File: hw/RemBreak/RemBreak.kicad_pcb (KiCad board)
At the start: 11 copper layers, 40 x 80 mm, 78 parts, among them IC1 LTC2943IDD#TRPBF, J1 Conn_01x03, J10 Screw_Terminal_01x02, J11 Conn_01x03, J2 Conn_02x06_Odd_Even, J3 Screw_Terminal_01x04, J5 Screw_Terminal_01x04, J8 Conn_01x07, J9 Conn_01x07, Q1 BC337, Q11 BC337, Q12 BC847, Q2 BC847, Q3 BC847, Q4 BC337, Q5 BC847, Q6 BC337, Q7 BC847, Q8 SiS415DNT, Q9 BC337, U1 L7805, U2 L7805, U3 XC6220B331MR, U4 MAX40200AUK, U5 INA219BxDCN, U7 MAX40200AUK, U8 BD48ExxG, U9 BD48ExxG

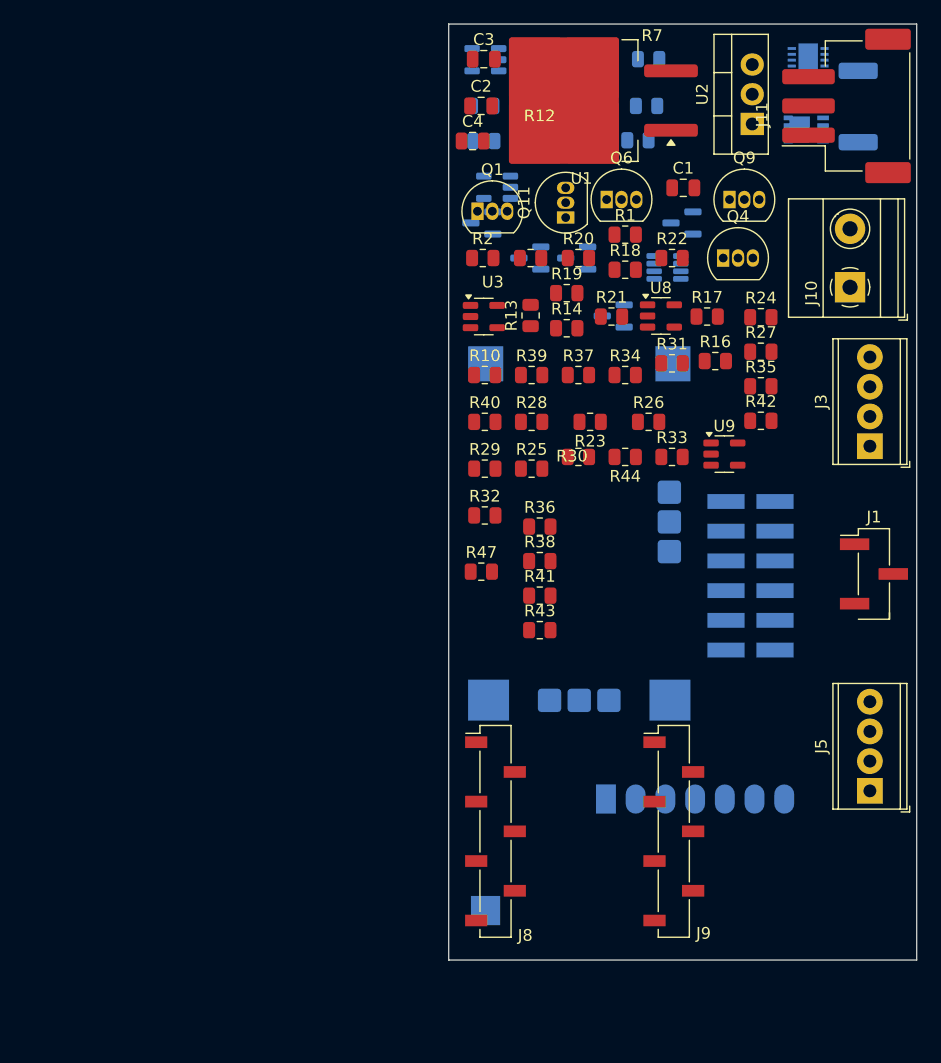
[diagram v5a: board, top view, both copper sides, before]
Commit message: created 3mm band around the pcb and components grouped to be easily placed in the final layout
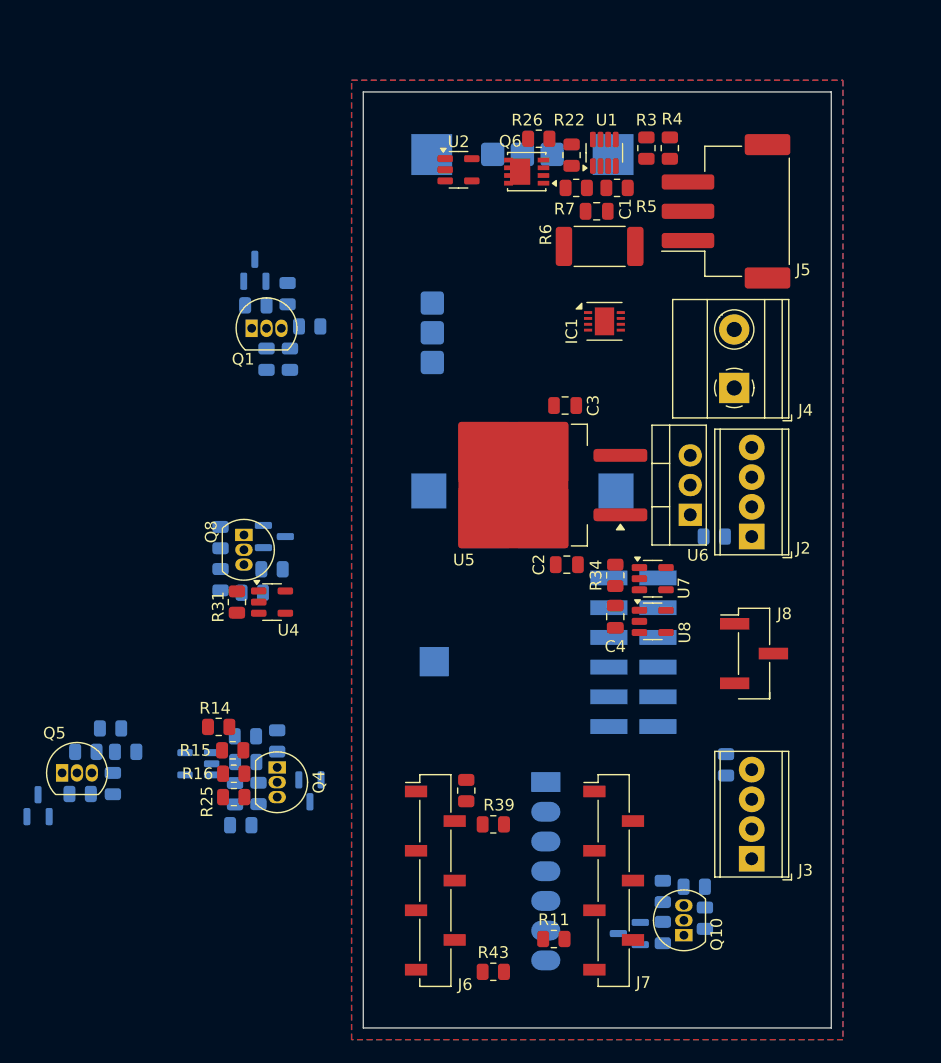
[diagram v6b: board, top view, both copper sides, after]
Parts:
- removed J11: Conn_01x03, Connector_JST:JST_XH_S3B-XH-SM4-TB_1x03-1MP_P2.50mm_Horizontal
- removed R47: 4k2, Resistor_SMD:R_0805_2012Metric
- added J5: Conn_01x03_MountingPin, Connector_JST:JST_XH_S3B-XH-SM4-TB_1x03-1MP_P2.50mm_Horizontal, F.Cu at (151.0, 70.2)
- IC1: moved to F.Cu
- Q6: renamed from Q8; moved to F.Cu
- R1, R2: moved to B.Cu
- R10: renamed from R19; moved to B.Cu
- R12: renamed from R20; moved to B.Cu
- R13: renamed from R21; moved to B.Cu
- R17: renamed from R31; moved to B.Cu
- R18: renamed from R25; moved to B.Cu
- R19: renamed from R33; moved to B.Cu
- R20: renamed from R36; moved to B.Cu
- R21: renamed from R37; moved to B.Cu
- R23: renamed from R35; moved to B.Cu
- R24: renamed from R28; moved to B.Cu
- R27: renamed from R40; moved to B.Cu
- R28: renamed from R34; moved to B.Cu
- R29: renamed from R38; moved to B.Cu
- R30: renamed from R39; moved to B.Cu
- R32: renamed from R43; moved to B.Cu
- R33: renamed from R44; moved to B.Cu
- R35: renamed from R42; moved to B.Cu
- R36: renamed from R41; moved to B.Cu
- R39: renamed from R6; moved to F.Cu
- R40: renamed from R7; moved to F.Cu
- R43: renamed from R11; moved to F.Cu
- R6: renamed from R15; moved to F.Cu
- R8: renamed from R17; moved to B.Cu
- R9: renamed from R18; moved to B.Cu
- U1: renamed from U5; moved to F.Cu
- U2: renamed from U7; moved to F.Cu
- U3: renamed from U8; moved to B.Cu
- U8: renamed from U4; moved to F.Cu
- moved R41 72.4 mm to (145.6, 131.8), turned to 90 degrees
- moved R43 72.1 mm to (131.1, 135.2), turned to 0 degrees
- moved R37 71.6 mm to (145.6, 128.3), turned to -90 degrees
- moved R42 69.6 mm to (149.2, 130.6), turned to 90 degrees
- moved R38 69.1 mm to (148.3, 127.9), turned to 0 degrees
- moved R40 64.4 mm to (128.8, 119.7), turned to -90 degrees
- moved Q10 64.3 mm to (147.4, 132.1), turned to 90 degrees
- moved Q5 64.1 mm to (94.3, 118.2), turned to 0 degrees
- moved Q7 62.6 mm to (92.2, 121.0), turned to 90 degrees
- moved R11 59.1 mm to (136.3, 132.4)
- moved R39 58.4 mm to (131.1, 122.6), turned to 0 degrees
- moved R15 58.4 mm to (108.8, 116.3), turned to 180 degrees
- moved Q11 58.4 mm to (142.7, 131.9)
- moved Q4 56.1 mm to (112.6, 117.7), turned to -90 degrees
- moved U3 55.0 mm to (105.9, 117.4), turned to 180 degrees
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- renumbered C4 to C1, C1 to C2, C2 to C3, C3 to C4, J2 to J1, J5 to J2, J10 to J4, J8 to J6, J9 to J7, J1 to J8, Q4 to Q1, Q1 to Q10, Q2 to Q11, Q5 to Q2, Q7 to Q3, Q6 to Q4, Q11 to Q5, Q12 to Q7, Q9 to Q8, Q3 to Q9, R22 to R11, R23 to R14, R24 to R15, R32 to R16, R26 to R22, R29 to R25, R27 to R26, R12 to R3, R30 to R31, R10 to R34, R4 to R37, R5 to R38, R13 to R4, R8 to R41, R9 to R42, R14 to R5, R16 to R7, U9 to U4, U1 to U5, U2 to U6, U3 to U7
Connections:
- net /VEXT renamed Net-(J2-Pin_3)
- J7 pad 1: unconnected-(J9-Pin_1-Pad1) -> /break_control/VBUS
- J7 pad 2: /break_control/BALARM -> GND
- J7 pad 3: /break_control/CHARGING -> +3V3
- J7 pad 5: +3V3 -> /break_control/CHARGING
- J7 pad 6: GND -> /break_control/BALARM
- J7 pad 7: /break_control/VBUS -> unconnected-(J7-Pin_7-Pad7)
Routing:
- added copper zone on B.Cu, net GND
- added copper zone on F.Cu, net GND
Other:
- board text removed: "- 3 (5)mm odstpu od kraju"
- board text removed: "- Connect schematics, check if the power symbols connect components across the whole schematics - connect missig wires to MCU and the 12pin connector"

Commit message: started routing of the pcb
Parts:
- C3, R14, R31, U4: moved to B.Cu
- R1, R10, R17, R18, R19, R21, R23, R24, R27, R28, R8, U3: moved to F.Cu
- moved Q7 65.0 mm to (124.9, 64.8), turned to 0 degrees
- moved R30 61.8 mm to (128.0, 64.8), turned to -90 degrees
- moved R29 56.9 mm to (124.0, 70.6), turned to 90 degrees
- moved Q5 56.8 mm to (125.8, 70.9), turned to 90 degrees
- moved R20 55.6 mm to (127.8, 70.6), turned to 90 degrees
- moved R21 55.6 mm to (129.0, 69.2), turned to 90 degrees
- moved R18 51.6 mm to (129.0, 72.8), turned to -90 degrees
- moved Q8 43.0 mm to (146.6, 120.1)
- moved R32 43.0 mm to (147.3, 125.1)
- moved R33 43.0 mm to (144.6, 124.0)
- moved R35 43.0 mm to (149.0, 123.1)
- moved R36 43.0 mm to (144.6, 120.4)
- moved Q9 43.0 mm to (149.2, 120.3)
- moved R31 41.7 mm to (143.8, 126.8), turned to 180 degrees
- moved U4 35.7 mm to (141.8, 123.6), turned to 90 degrees
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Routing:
- net +7.5V: track 0.00 -> 43.7 mm
- net +3V3: track 0.00 -> 25.9 mm
- net Net-(Q5-C): track 0.00 -> 18.9 mm, vias 0 -> 1
- net /power_manager/CHARGED (GREEN): track 0.00 -> 8.84 mm
- net Net-(Q1-B): track 0.00 -> 8.35 mm
- net Net-(Q5-B): track 0.00 -> 7.70 mm
- net Net-(Q5-E): track 0.00 -> 7.08 mm
- net +5V: track 0.00 -> 5.85 mm
- net /break_control/CHARGING: track 0.00 -> 4.47 mm
- net Net-(Q1-E): track 0.00 -> 3.64 mm
- net /break_control/I2C.SDA: track 0.00 -> 3.59 mm
- net /break_control/I2C.SCL: track 0.00 -> 2.76 mm
- net Net-(U3-VOUT): track 0.00 -> 1.65 mm, vias 0 -> 1
- net Net-(J5-Pin_2): vias 0 -> 1
- net /power_manager/VBATT: vias 0 -> 1
- added copper zone on F.Cu, net +3V3
- added copper zone on F.Cu, net +7.5V
- added copper zone on B.Cu, net /power_manager/VBATT
- added copper zone on F.Cu, net /power_manager/VBATT
- added copper zone on F.Cu, net Net-(IC1-SENSE-)
- added copper zone on B.Cu, net Net-(J5-Pin_2)
- added copper zone on B.Cu, net Net-(Q1-E)
- added copper zone on B.Cu, net Net-(Q5-C)
- added copper zone on F.Cu, net Net-(Q5-E)
- added copper zone on F.Cu, net Net-(Q6-G)
- added copper zone on F.Cu, net Net-(U1-IN+)
- added copper zone on F.Cu, net Net-(U1-IN-)
- added copper zone on B.Cu, net Net-(U3-VOUT)
- added copper zone on F.Cu, net Net-(U3-VOUT)
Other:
- copper layers 11 -> 2

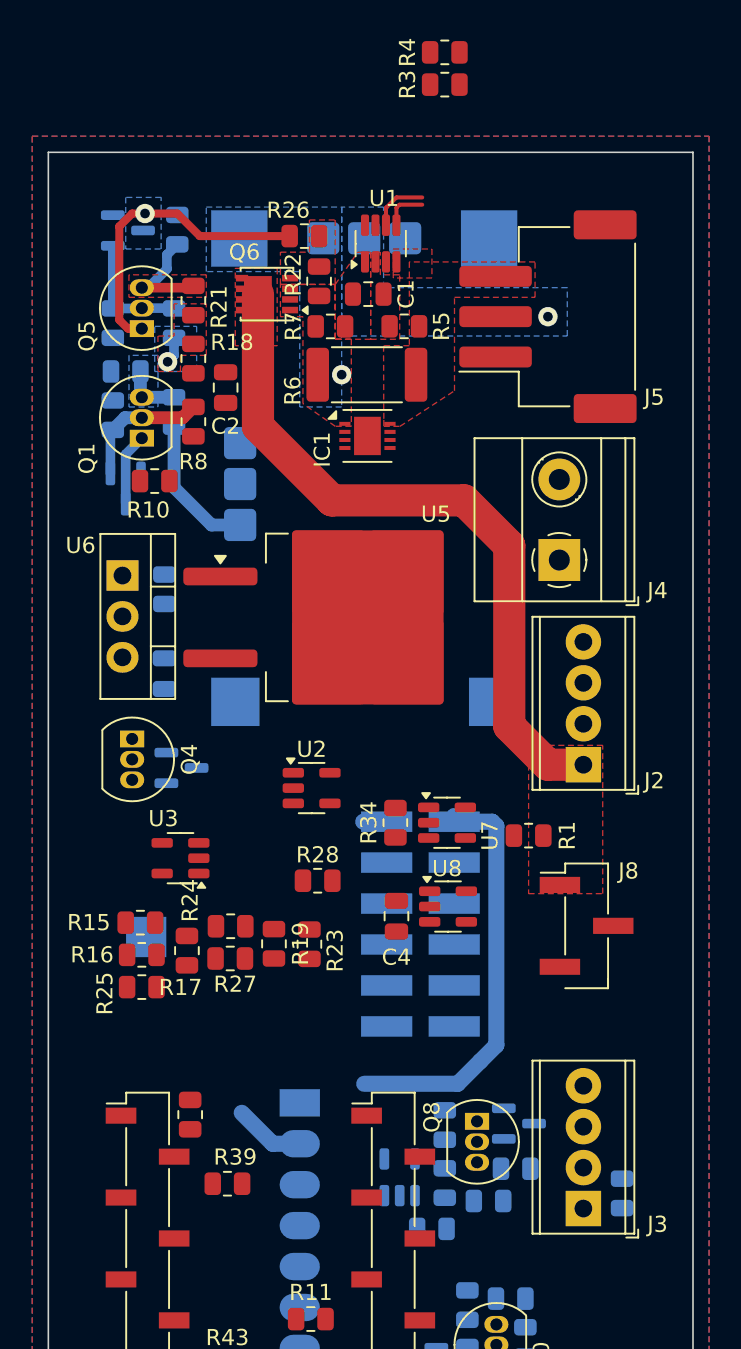
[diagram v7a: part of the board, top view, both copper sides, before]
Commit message: routing in progress added new subsheet to easily swap signals at the control connector
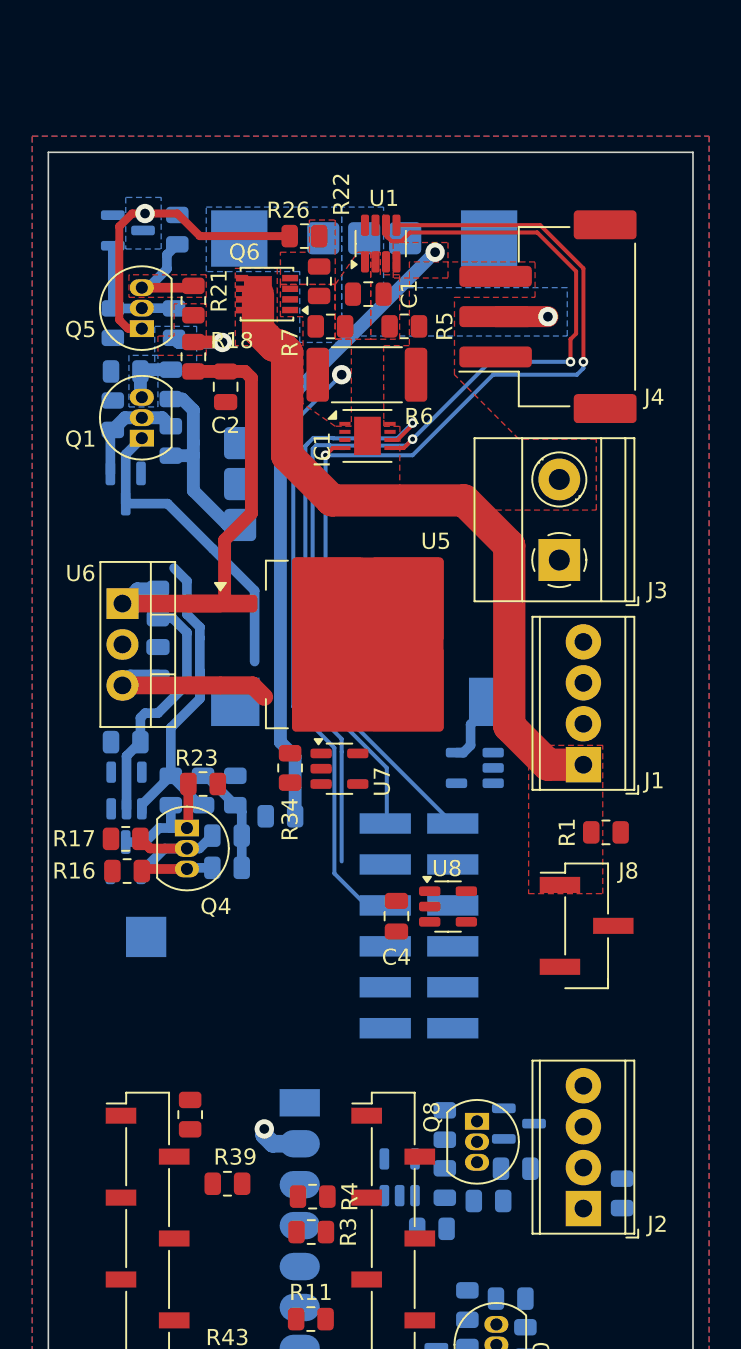
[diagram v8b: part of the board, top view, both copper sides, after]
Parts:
- removed the J1 at (149.5, 107.9)
- added J5: Conn_02x06_Odd_Even, chinese_modules:SAMTEC_TSM-106-01-L-DH-P-TR, B.Cu at (149.4, 108.0)
- R10, R15, R19, R24, R25, R27, R28, R8, U2, U3: moved to B.Cu
- moved R3 71.7 mm to (136.3, 127.0), turned to 180 degrees
- moved R4 71.5 mm to (136.4, 124.8), turned to 180 degrees
- moved R10 22.2 mm to (134.4, 101.2)
- moved R23 11.9 mm to (129.6, 99.2), turned to 180 degrees
- moved R19 11.5 mm to (127.6, 99.6), turned to 90 degrees
- moved R15 11.2 mm to (124.8, 96.6), turned to 0 degrees
- moved R27 10.6 mm to (129.6, 99.6), turned to -90 degrees
- moved U2 10.2 mm to (146.5, 98.2), turned to 180 degrees
- moved R25 9.09 mm to (131.1, 104.4), turned to 180 degrees
- moved R17 7.91 mm to (124.8, 102.6), turned to 0 degrees
- moved R28 7.58 mm to (131.6, 99.6), turned to -90 degrees
- moved U7 7.47 mm to (138.1, 98.2)
- moved R34 7.37 mm to (135.0, 98.2)
- moved Q3 6.53 mm to (124.8, 103.7), turned to 90 degrees
- moved Q4 6.49 mm to (128.6, 101.9)
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- renumbered J2 to J1, J3 to J2, J4 to J3, J5 to J4
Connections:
- net /break_control/CHARGING renamed /control_connector/LED BLUE
- net /power_manager/CHARGED (GREEN) renamed /control_connector/LED GREEN
- net /power_manager/VBATT renamed /control_connector/VBATT
- net /power_switch/ON/OFF renamed /control_connector/ONOFF
- net /power_switch/RUNNIG (RED) renamed /control_connector/LED RED
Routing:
- net /break_control/I2C.SDA: track 3.59 -> 66.3 mm, vias 0 -> 2
- net /break_control/I2C.SCL: track 2.76 -> 64.7 mm, vias 0 -> 2
- net /control_connector/VBATT: track 0.00 -> 37.2 mm
- net /break_control/BALARM: track 0.00 -> 35.9 mm, vias 0 -> 1
- net /control_connector/ONOFF: track 0.00 -> 27.2 mm
- net Net-(U3-VOUT): track 1.65 -> 26.6 mm
- net Net-(U3-VDD): track 0.00 -> 15.4 mm
- net /control_connector/LED BLUE: track 4.47 -> 19.1 mm
- net +3V3: track 25.9 -> 39.4 mm, vias 0 -> 1
- net Net-(Q3-B): track 0.00 -> 8.50 mm
- net +5V: track 5.85 -> 14.3 mm, vias 0 -> 1
- net Net-(Q3-C): track 0.00 -> 8.34 mm
- net Net-(R24-Pad1): track 0.00 -> 6.81 mm
- net Net-(Q4-E): track 0.00 -> 4.46 mm
- net Net-(M1-Vin): track 0.00 -> 4.34 mm
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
